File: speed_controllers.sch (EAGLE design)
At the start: 47 parts, among them M1 TE-1-1123723-3, M2 TE-1-1123723-3, M3 TE-1-1123723-3, M4 TE-1-1123723-3, M5 TE-1-1123723-3, M6 TE-1-1123723-3, M7 TE-1-1123723-3, M8 TE-1-1123723-3

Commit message: Changed board to not have anything within a 5 inch diameter on the back side
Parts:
- added R10: 10k, auv:R-US_R0603
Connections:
- new net N$4: OK1.A, R10.1
- net VCC: now also R10.2; no longer OK1.A
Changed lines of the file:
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@@
 <?xml version="1.0" encoding="utf-8"?>
 <!DOCTYPE eagle SYSTEM "eagle.dtd">
-<eagle version="8.6.1">
+<eagle version="9.0.0">
 <drawing>
 <settings>
@@
 <part name="GND16" library="auv" deviceset="GND" device=""/>
 <part name="C1" library="rcl" library_urn="urn:adsk.eagle:library:334" deviceset="C-EU" device="C0603" package3d_urn="urn:adsk.eagle:package:23616/2" value="100nF"/>
+<part name="R10" library="auv" deviceset="R-US_" device="R0603" value="10k"/>
 </parts>
 <sheets>
@@
 <instance part="JP1" gate="A" x="35.56" y="-71.12" rot="R270"/>
 <instance part="OK1" gate="A" x="88.9" y="-111.76"/>
-<instance part="SUPPLY10" gate="G$1" x="71.12" y="-93.98"/>
+<instance part="SUPPLY10" gate="G$1" x="66.04" y="-99.06"/>
 <instance part="FET1" gate="G$1" x="-2.54" y="-27.94" rot="R180"/>
 <instance part="FET2" gate="G$1" x="-2.54" y="35.56" rot="R180"/>
@@
 <instance part="GND16" gate="1" x="96.52" y="-33.02"/>
 <instance part="C1" gate="G$1" x="83.82" y="-76.2"/>
+<instance part="R10" gate="G$1" x="71.12" y="-106.68" rot="R180"/>
 </instances>
 <busses>
@@
 </segment>
 <segment>
-<pinref part="SUPPLY1" gate="G$1" pin="VCC"/>
-<wire x1="-2.54" y1="43.18" x2="-2.54" y2="40.64" width="0.1524" layer="91"/>
-<pinref part="FET2" gate="G$1" pin="S"/>
-</segment>
-<segment>
 <pinref part="SUPPLY2" gate="G$1" pin="VCC"/>
 <wire x1="-2.54" y1="99.06" x2="-2.54" y2="96.52" width="0.1524" layer="91"/>
@@
 <segment>
 <pinref part="SUPPLY10" gate="G$1" pin="VCC"/>
-<pinref part="OK1" gate="A" pin="A"/>
-<wire x1="71.12" y1="-96.52" x2="71.12" y2="-106.68" width="0.1524" layer="91"/>
-<wire x1="76.2" y1="-106.68" x2="71.12" y2="-106.68" width="0.1524" layer="91"/>
+<pinref part="R10" gate="G$1" pin="2"/>
+<wire x1="66.04" y1="-101.6" x2="66.04" y2="-106.68" width="0.1524" layer="91"/>
+</segment>
+<segment>
+<pinref part="FET2" gate="G$1" pin="S"/>
+<pinref part="SUPPLY1" gate="G$1" pin="VCC"/>
+<wire x1="-2.54" y1="40.64" x2="-2.54" y2="43.18" width="0.1524" layer="91"/>
 </segment>
 </net>
@@
 </segment>
 </net>
+<net name="N$4" class="0">
+<segment>
+<pinref part="OK1" gate="A" pin="A"/>
+<pinref part="R10" gate="G$1" pin="1"/>
+</segment>
+</net>

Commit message: Fix silkscreen
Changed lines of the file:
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@@
 <?xml version="1.0" encoding="utf-8"?>
 <!DOCTYPE eagle SYSTEM "eagle.dtd">
-<eagle version="9.0.0">
+<eagle version="9.0.1">
 <drawing>
 <settings>

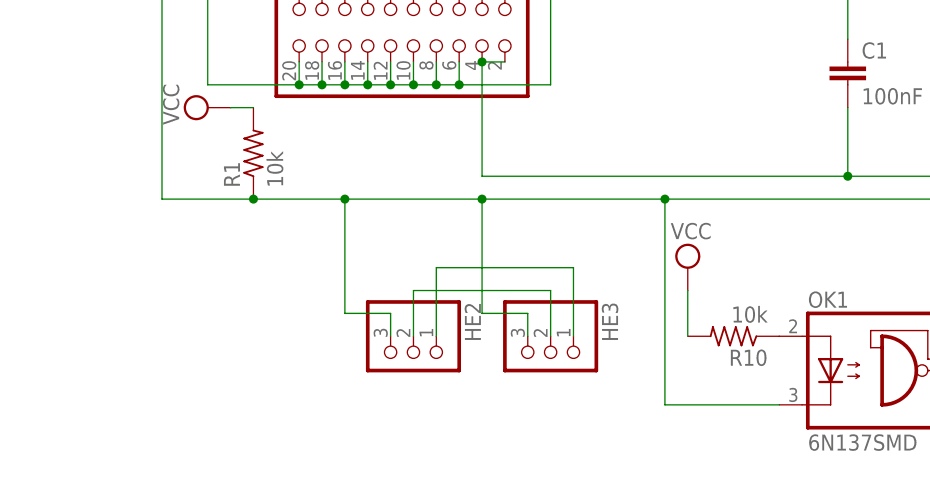
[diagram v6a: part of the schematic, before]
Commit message: Add another hall effect and fix resistor value
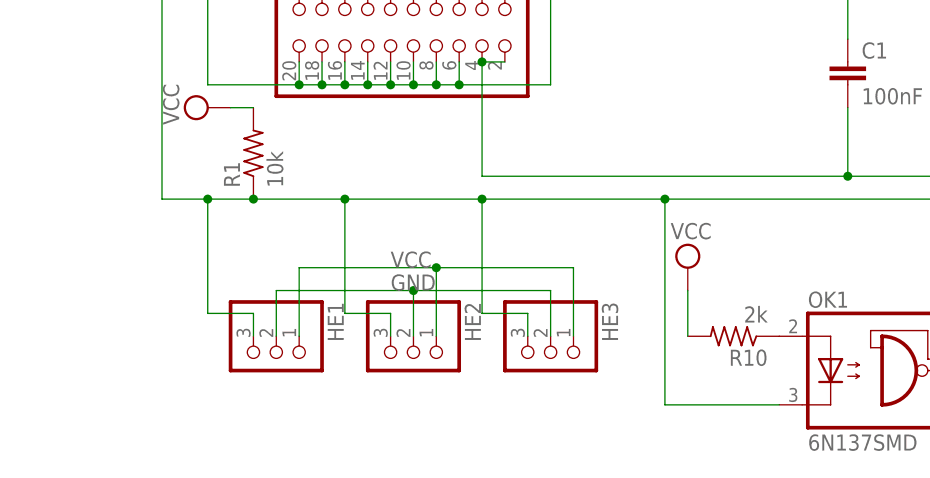
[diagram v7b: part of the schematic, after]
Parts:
- added HE1: (no value), auv:PINHD-1X3
- R10: value 10k -> 2k
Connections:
- net FET_G: now also HE1.3
- net GND: now also HE1.2
- net VCC: now also HE1.1
